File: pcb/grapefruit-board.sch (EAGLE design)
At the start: 151 parts, among them IC1 L70, IC10 TS520525, IC2 STC3100, IC3 TPS61200, IC4 LM3671MF, IC5 MCP73837MF, IC6 LM2840/1/2, IC7 STM32F411XC, IC8 S25FL064K, IC9 TLV320AIC3100, M1 ELECTRET_MICROPHON-WM-62PC/62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, Q1 BSS84, Q2 BSS84, Q3 BSS84, Q4 BSS84, X1 BU-SMA-V, X2 BU-SMA-V, X3 BU-SMA-V, X4 USB-MICROB, X5 USB-MICROB, Y1 32768Hz

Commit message: Change values of some components, add SWD pin header
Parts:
- added JP10: (no value), pinhead:PINHD-1X4
- C46, C47: value 12pF -> 22pF
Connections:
- removed net N$53: C55.1, IC7.NRST
- new net NRST: C55.1, IC7.NRST, JP10.4
- new net SWCLK: IC7.PA14, JP10.2
- new net SWDIO: IC7.PA13, JP10.1
- new net USART1_RX: IC7.PB3
- new net USART1_TX: IC7.PA15
- net GND: now also JP10.3, JP4.1; no longer JP4.2
- net N$10: now also JP4.2; no longer JP4.1
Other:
- note added: "(c) 2016 Marek Koza, qyx@krtko.org, CC-BY-SA"
- note added: "version 1.0.0-a.1+20160428"
- moved on the sheet: JP4
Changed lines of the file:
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@@
 <part name="GND62" library="supply1" deviceset="GND" device=""/>
 <part name="U$1" library="qyx-misc" deviceset="XTAL-7M" device=""/>
-<part name="C46" library="rcl" deviceset="C-EU" device="C0603" value="12pF"/>
-<part name="C47" library="rcl" deviceset="C-EU" device="C0603" value="12pF"/>
+<part name="C46" library="rcl" deviceset="C-EU" device="C0603" value="22pF"/>
+<part name="C47" library="rcl" deviceset="C-EU" device="C0603" value="22pF"/>
 <part name="R32" library="rcl" deviceset="R-EU_" device="R0603" value="47K"/>
 <part name="C48" library="rcl" deviceset="C-EU" device="C0805" value="2.2uF"/>
@@
 <part name="GND3" library="supply1" deviceset="GND" device=""/>
 <part name="C58" library="rcl" deviceset="C-EU" device="C0603" value="100nF"/>
+<part name="JP10" library="pinhead" deviceset="PINHD-1X4" device=""/>
+<part name="GND68" library="supply1" deviceset="GND" device=""/>
 </parts>
 <sheets>
@@
 <text x="525.78" y="7.62" size="1.778" layer="97">Audio I2S codec</text>
 <text x="360.68" y="360.68" size="1.778" layer="97">Radio modules</text>
+<text x="17.78" y="-127" size="1.778" layer="97">(c) 2016 Marek Koza, qyx@krtko.org, CC-BY-SA</text>
+<text x="17.78" y="-129.54" size="1.778" layer="97">version 1.0.0-a.1+20160428</text>
+<wire x1="627.38" y1="340.36" x2="688.34" y2="340.36" width="0.1524" layer="97"/>
+<wire x1="688.34" y1="340.36" x2="688.34" y2="299.72" width="0.1524" layer="97"/>
+<wire x1="688.34" y1="299.72" x2="627.38" y2="299.72" width="0.1524" layer="97"/>
+<wire x1="627.38" y1="299.72" x2="627.38" y2="340.36" width="0.1524" layer="97"/>
 </plain>
 <instances>
@@
 <instance part="JP3" gate="1" x="731.52" y="109.22"/>
 <instance part="JP5" gate="G$1" x="513.08" y="76.2" rot="MR0"/>
-<instance part="JP4" gate="G$1" x="576.58" y="76.2" rot="R180"/>
+<instance part="JP4" gate="G$1" x="576.58" y="73.66" rot="MR0"/>
 <instance part="JP6" gate="G$1" x="571.5" y="129.54"/>
 <instance part="+3V10" gate="G$1" x="741.68" y="109.22"/>
@@
 <instance part="GND3" gate="1" x="561.34" y="312.42"/>
 <instance part="C58" gate="G$1" x="375.92" y="5.08"/>
+<instance part="JP10" gate="A" x="673.1" y="320.04"/>
+<instance part="GND68" gate="1" x="662.94" y="309.88"/>
 </instances>
 <busses>
@@
 </segment>
 <segment>
-<pinref part="JP4" gate="G$1" pin="2"/>
 <pinref part="GND35" gate="1" pin="GND"/>
-<wire x1="568.96" y1="73.66" x2="566.42" y2="73.66" width="0.1524" layer="91"/>
 <wire x1="566.42" y1="73.66" x2="566.42" y2="71.12" width="0.1524" layer="91"/>
+<pinref part="JP4" gate="G$1" pin="1"/>
+<wire x1="566.42" y1="73.66" x2="568.96" y2="73.66" width="0.1524" layer="91"/>
 </segment>
 <segment>
@@
 <wire x1="561.34" y1="327.66" x2="561.34" y2="317.5" width="0.1524" layer="91"/>
 <junction x="561.34" y="317.5"/>
+</segment>
+<segment>
+<pinref part="JP10" gate="A" pin="3"/>
+<pinref part="GND68" gate="1" pin="GND"/>
+<wire x1="670.56" y1="320.04" x2="662.94" y2="320.04" width="0.1524" layer="91"/>
+<wire x1="662.94" y1="320.04" x2="662.94" y2="312.42" width="0.1524" layer="91"/>
 </segment>
 </net>
@@
 <pinref part="JP2" gate="1" pin="3"/>
 <wire x1="566.42" y1="83.82" x2="566.42" y2="76.2" width="0.1524" layer="91"/>
-<pinref part="JP4" gate="G$1" pin="1"/>
-<wire x1="566.42" y1="76.2" x2="568.96" y2="76.2" width="0.1524" layer="91"/>
+<pinref part="JP4" gate="G$1" pin="2"/>
+<wire x1="568.96" y1="76.2" x2="566.42" y2="76.2" width="0.1524" layer="91"/>
 </segment>
 </net>
@@
 <segment>
 <pinref part="IC7" gate="G$1" pin="PA12"/>
-<wire x1="436.88" y1="-48.26" x2="452.12" y2="-48.26" width="0.1524" layer="91"/>
-<label x="452.12" y="-48.26" size="1.778" layer="95" xref="yes"/>
+<wire x1="436.88" y1="-48.26" x2="459.74" y2="-48.26" width="0.1524" layer="91"/>
+<label x="459.74" y="-48.26" size="1.778" layer="95" xref="yes"/>
 </segment>
 <segment>
@@
 </segment>
 </net>
-<net name="N$53" class="0">
+<net name="NRST" class="0">
 <segment>
 <pinref part="C55" gate="G$1" pin="1"/>
 <wire x1="408.94" y1="7.62" x2="408.94" y2="10.16" width="0.1524" layer="91"/>
 <wire x1="408.94" y1="10.16" x2="388.62" y2="10.16" width="0.1524" layer="91"/>
-<wire x1="388.62" y1="10.16" x2="388.62" y2="-20.32" width="0.1524" layer="91"/>
+<wire x1="388.62" y1="10.16" x2="388.62" y2="2.54" width="0.1524" layer="91"/>
 <pinref part="IC7" gate="G$1" pin="NRST"/>
+<wire x1="388.62" y1="2.54" x2="388.62" y2="-20.32" width="0.1524" layer="91"/>
 <wire x1="388.62" y1="-20.32" x2="391.16" y2="-20.32" width="0.1524" layer="91"/>
+<wire x1="388.62" y1="2.54" x2="391.16" y2="2.54" width="0.1524" layer="91"/>
+<junction x="388.62" y="2.54"/>
+<label x="391.16" y="2.54" size="1.778" layer="95" xref="yes"/>
+</segment>
+<segment>
+<pinref part="JP10" gate="A" pin="4"/>
+<wire x1="670.56" y1="317.5" x2="660.4" y2="317.5" width="0.1524" layer="91"/>
+<label x="660.4" y="317.5" size="1.778" layer="95" rot="R180" xref="yes"/>
 </segment>
 </net>
@@
 </segment>
 </net>
+<net name="USART1_TX" class="0">
+<segment>
+<pinref part="IC7" gate="G$1" pin="PA15"/>
+<wire x1="436.88" y1="-55.88" x2="441.96" y2="-55.88" width="0.1524" layer="91"/>
+<label x="441.96" y="-55.88" size="1.778" layer="95" xref="yes"/>
+</segment>
+</net>
+<net name="USART1_RX" class="0">
+<segment>
+<pinref part="IC7" gate="G$1" pin="PB3"/>
+<wire x1="436.88" y1="-71.12" x2="454.66" y2="-71.12" width="0.1524" layer="91"/>
+<label x="454.66" y="-71.12" size="1.778" layer="95" xref="yes"/>
+</segment>
+</net>
+<net name="SWDIO" class="0">
+<segment>
+<pinref part="IC7" gate="G$1" pin="PA13"/>
+<wire x1="436.88" y1="-50.8" x2="441.96" y2="-50.8" width="0.1524" layer="91"/>
+<label x="441.96" y="-50.8" size="1.778" layer="95" xref="yes"/>
+</segment>
+<segment>
+<pinref part="JP10" gate="A" pin="1"/>
+<wire x1="670.56" y1="325.12" x2="662.94" y2="325.12" width="0.1524" layer="91"/>
+<label x="662.94" y="325.12" size="1.778" layer="95" rot="R180" xref="yes"/>
+</segment>
+</net>
+<net name="SWCLK" class="0">
+<segment>
+<pinref part="IC7" gate="G$1" pin="PA14"/>
+<wire x1="436.88" y1="-53.34" x2="459.74" y2="-53.34" width="0.1524" layer="91"/>
+<label x="459.74" y="-53.34" size="1.778" layer="95" xref="yes"/>
+</segment>
+<segment>
+<pinref part="JP10" gate="A" pin="2"/>
+<wire x1="670.56" y1="322.58" x2="650.24" y2="322.58" width="0.1524" layer="91"/>
+<label x="650.24" y="322.58" size="1.778" layer="95" rot="R180" xref="yes"/>
+</segment>
+</net>

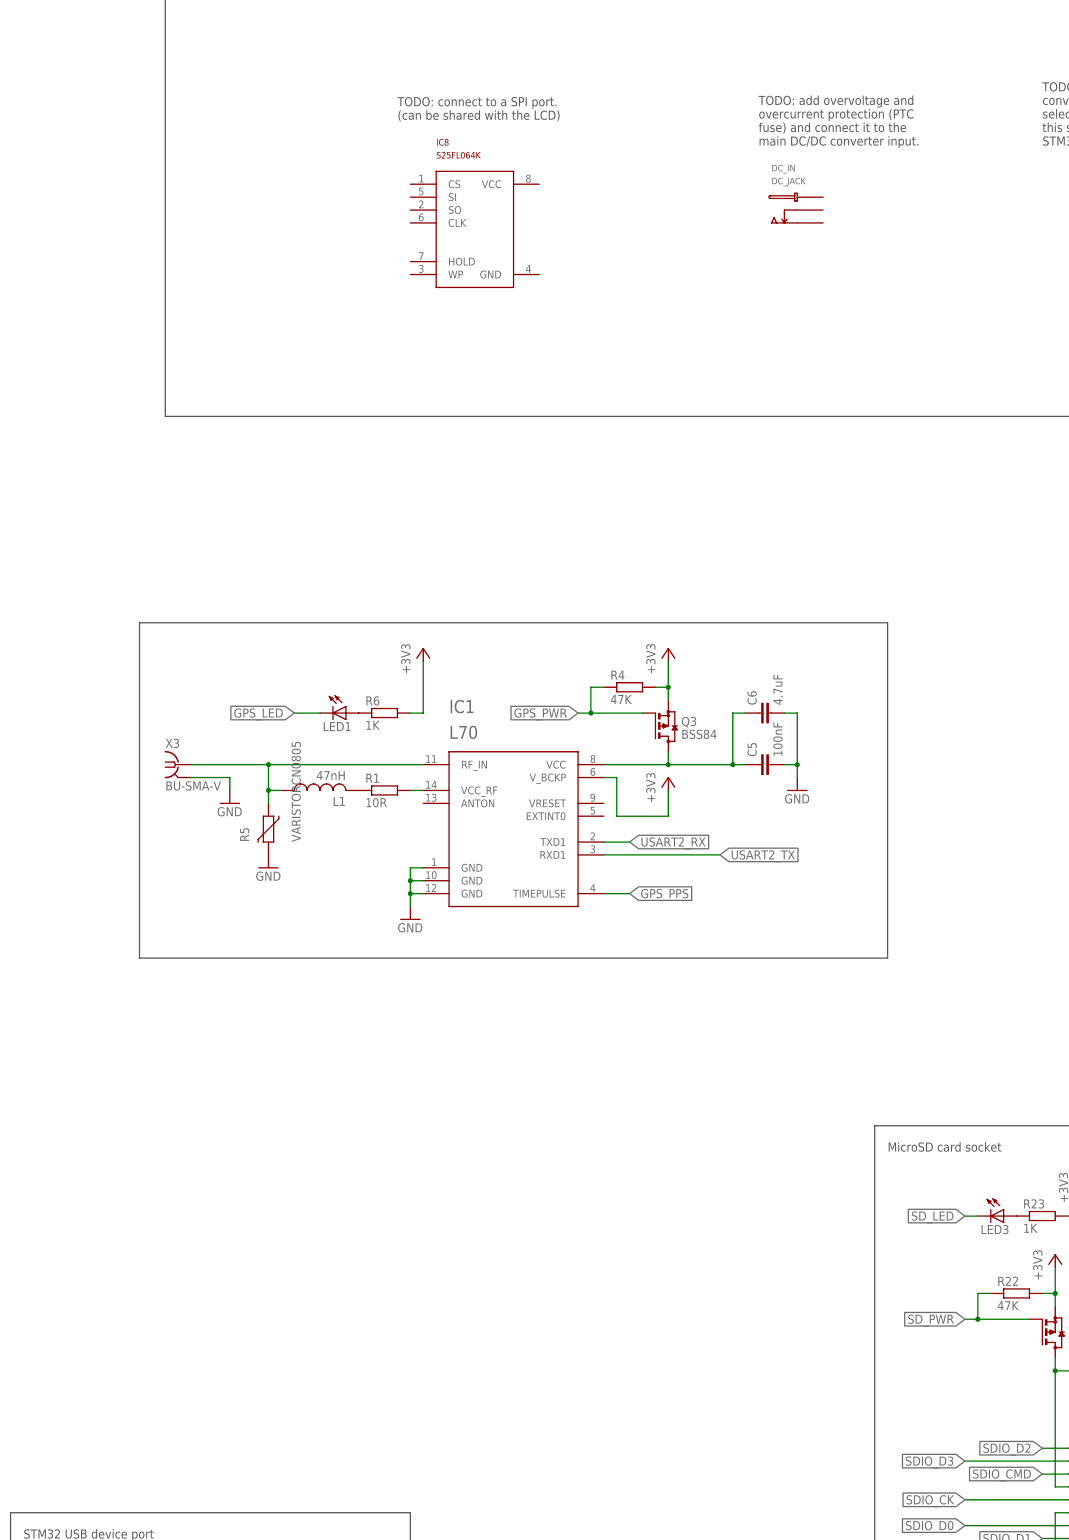
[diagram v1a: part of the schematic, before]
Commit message: Add DC IN input
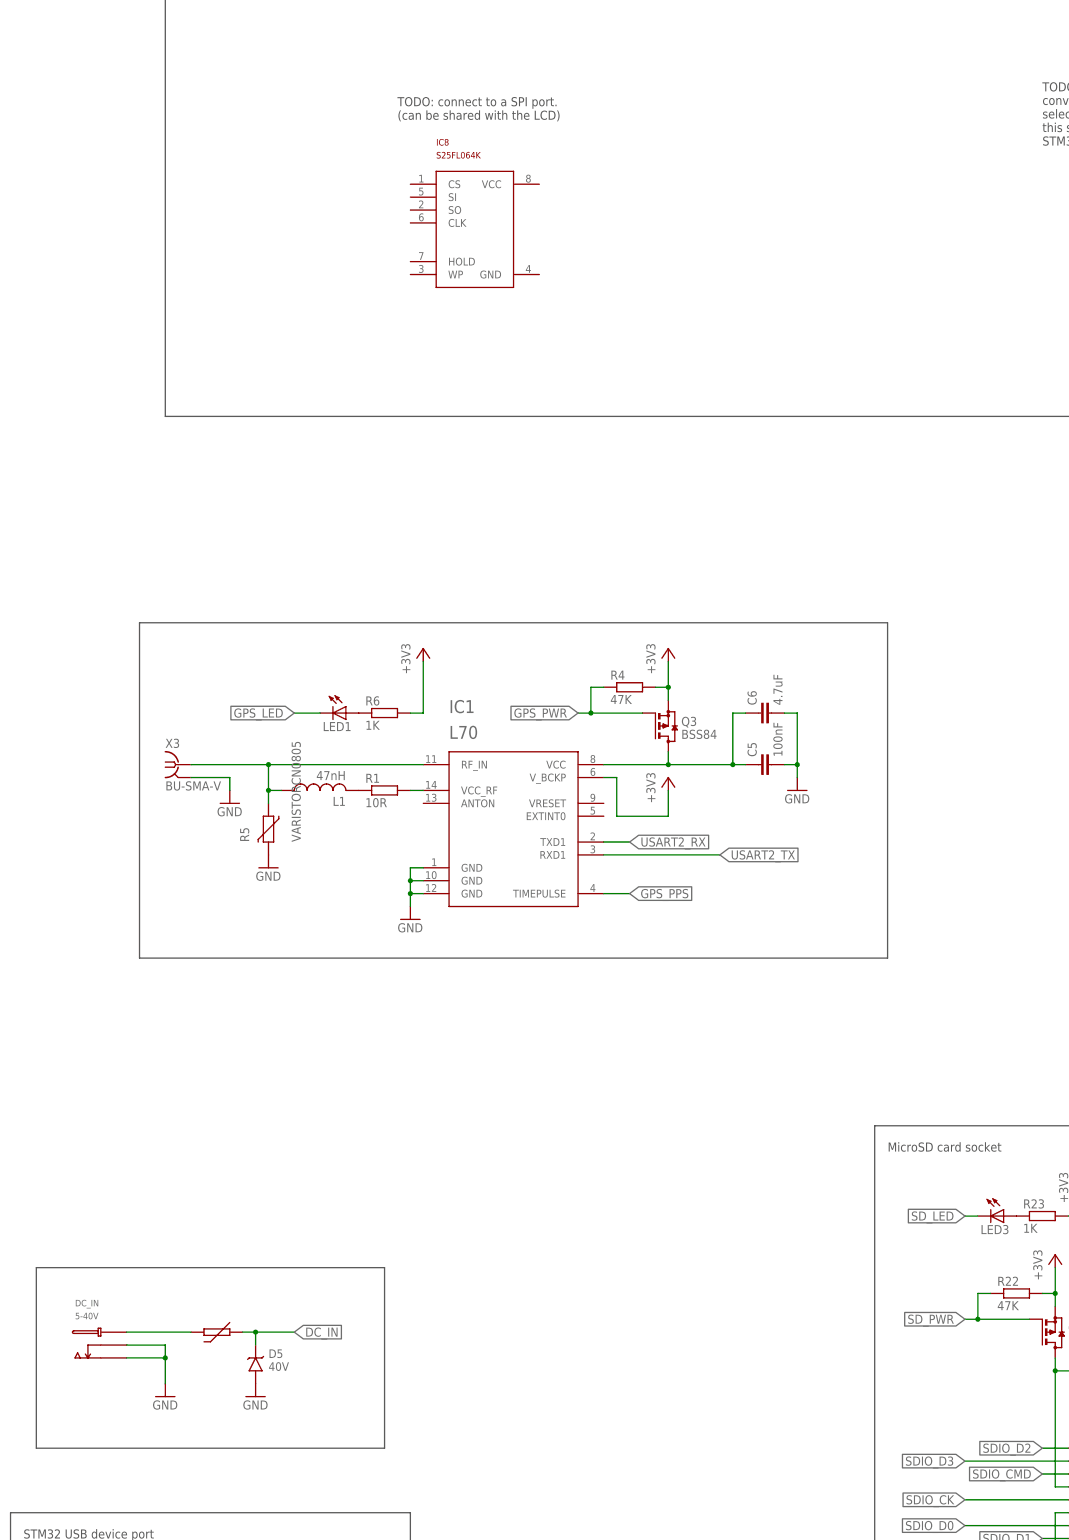
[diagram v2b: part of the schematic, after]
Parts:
- added D5: 40V, qyx-misc:DIODE_TVS_SMA
- added U$2: PTC_FUSE1210, qyx-misc:PTC_FUSE1210
- DC_IN: value DC_JACK -> 5-40V
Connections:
- new net N$53: DC_IN.C, U$2.1
- net DC_IN: now also D5.K, U$2.2
- net GND: now also D5.A, DC_IN.O, DC_IN.OSW
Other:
- note removed: "TODO: add overvoltage and overcurrent protection (PTC fuse) and connect it to the main DC/DC converter input."
- moved on the sheet: DC_IN
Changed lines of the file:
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@@
 <part name="MIC" library="qyx-misc" deviceset="MJ-2135" device=""/>
 <part name="GND11" library="supply1" deviceset="GND" device=""/>
-<part name="DC_IN" library="con-qyx" deviceset="DC_JACK" device=""/>
+<part name="DC_IN" library="con-qyx" deviceset="DC_JACK" device="" value="5-40V"/>
 <part name="M1" library="microphon" deviceset="ELECTRET_MICROPHON-" device="WM-62PC/62PK" value="ELECTRET_MICROPHON-WM-62PC/62PK">
 <attribute name="PN" value="PMOF-6027PN-42UQ"/>
@@
 <part name="JP10" library="pinhead" deviceset="PINHD-1X4" device=""/>
 <part name="GND68" library="supply1" deviceset="GND" device=""/>
+<part name="U$2" library="qyx-misc" deviceset="PTC_FUSE" device="1210"/>
+<part name="GND69" library="supply1" deviceset="GND" device=""/>
+<part name="D5" library="qyx-misc" deviceset="DIODE_TVS_SMA" device="" value="40V"/>
+<part name="GND70" library="supply1" deviceset="GND" device=""/>
 </parts>
 <sheets>
@@
 <wire x1="7.62" y1="185.42" x2="7.62" y2="363.22" width="0.1524" layer="97"/>
 <text x="10.16" y="358.14" size="1.778" layer="97">TODO area</text>
-<text x="124.46" y="238.76" size="1.778" layer="97">TODO: add overvoltage and
-overcurrent protection (PTC
-fuse) and connect it to the
-main DC/DC converter input.</text>
 <text x="180.34" y="238.76" size="1.778" layer="97">TODO: a suitable USB-&gt;serial
 converter chip has to be
@@
 <wire x1="688.34" y1="299.72" x2="627.38" y2="299.72" width="0.1524" layer="97"/>
 <wire x1="627.38" y1="299.72" x2="627.38" y2="340.36" width="0.1524" layer="97"/>
+<wire x1="-17.78" y1="17.78" x2="50.8" y2="17.78" width="0.1524" layer="97"/>
+<wire x1="50.8" y1="17.78" x2="50.8" y2="-17.78" width="0.1524" layer="97"/>
+<wire x1="50.8" y1="-17.78" x2="-17.78" y2="-17.78" width="0.1524" layer="97"/>
+<wire x1="-17.78" y1="-17.78" x2="-17.78" y2="17.78" width="0.1524" layer="97"/>
 </plain>
 <instances>
@@
 <instance part="MIC" gate="G$1" x="726.44" y="-48.26" rot="R180"/>
 <instance part="GND11" gate="1" x="713.74" y="-58.42"/>
-<instance part="DC_IN" gate="G$1" x="127" y="228.6"/>
+<instance part="DC_IN" gate="G$1" x="-10.16" y="5.08"/>
 <instance part="M1" gate="G$1" x="711.2" y="-91.44" smashed="yes">
 <attribute name="PN" x="718.82" y="-91.44" size="1.778" layer="96" display="off"/>
@@
 <instance part="JP10" gate="A" x="673.1" y="320.04"/>
 <instance part="GND68" gate="1" x="662.94" y="309.88"/>
+<instance part="U$2" gate="G$1" x="17.78" y="5.08"/>
+<instance part="GND69" gate="1" x="7.62" y="-7.62"/>
+<instance part="D5" gate="G$1" x="25.4" y="2.54"/>
+<instance part="GND70" gate="1" x="25.4" y="-7.62"/>
 </instances>
 <busses>
@@
 <wire x1="662.94" y1="320.04" x2="662.94" y2="312.42" width="0.1524" layer="91"/>
 </segment>
+<segment>
+<pinref part="DC_IN" gate="G$1" pin="O"/>
+<pinref part="GND69" gate="1" pin="GND"/>
+<wire x1="0" y1="0" x2="7.62" y2="0" width="0.1524" layer="91"/>
+<wire x1="7.62" y1="0" x2="7.62" y2="-5.08" width="0.1524" layer="91"/>
+<pinref part="DC_IN" gate="G$1" pin="OSW"/>
+<wire x1="0" y1="2.54" x2="7.62" y2="2.54" width="0.1524" layer="91"/>
+<wire x1="7.62" y1="2.54" x2="7.62" y2="0" width="0.1524" layer="91"/>
+<junction x="7.62" y="0"/>
+</segment>
+<segment>
+<pinref part="D5" gate="G$1" pin="A"/>
+<pinref part="GND70" gate="1" pin="GND"/>
+</segment>
 </net>
 <net name="N$3" class="0">
@@
 <junction x="269.24" y="142.24"/>
 </segment>
+<segment>
+<pinref part="U$2" gate="G$1" pin="2"/>
+<pinref part="D5" gate="G$1" pin="K"/>
+<wire x1="22.86" y1="5.08" x2="25.4" y2="5.08" width="0.1524" layer="91"/>
+<wire x1="25.4" y1="5.08" x2="25.4" y2="2.54" width="0.1524" layer="91"/>
+<wire x1="25.4" y1="5.08" x2="33.02" y2="5.08" width="0.1524" layer="91"/>
+<junction x="25.4" y="5.08"/>
+<label x="33.02" y="5.08" size="1.778" layer="95" xref="yes"/>
+</segment>
 </net>
 <net name="VDD45" class="0">
@@
 </segment>
 </net>
+<net name="N$53" class="0">
+<segment>
+<pinref part="DC_IN" gate="G$1" pin="C"/>
+<pinref part="U$2" gate="G$1" pin="1"/>
+<wire x1="0" y1="5.08" x2="12.7" y2="5.08" width="0.1524" layer="91"/>
+</segment>
+</net>
